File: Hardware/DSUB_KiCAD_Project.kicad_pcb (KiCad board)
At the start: 4 copper layers, 112.2 x 87.2 mm, 6 parts, among them J1 DB37_Female, J11 DB37_Female, J3 DB37_Female, J5 DB37_Female, J7 DB37_Female, J9 DB37_Female

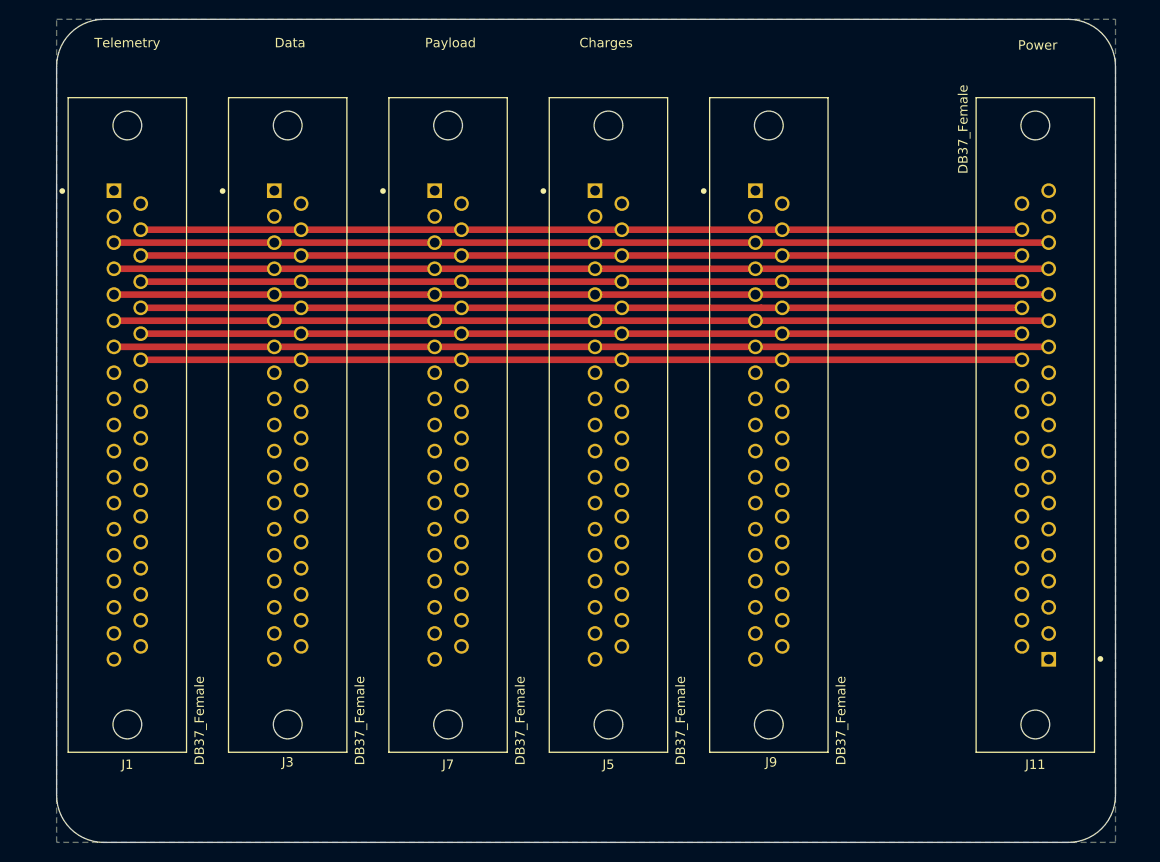
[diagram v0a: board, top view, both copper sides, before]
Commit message: Added more silk screen artwork
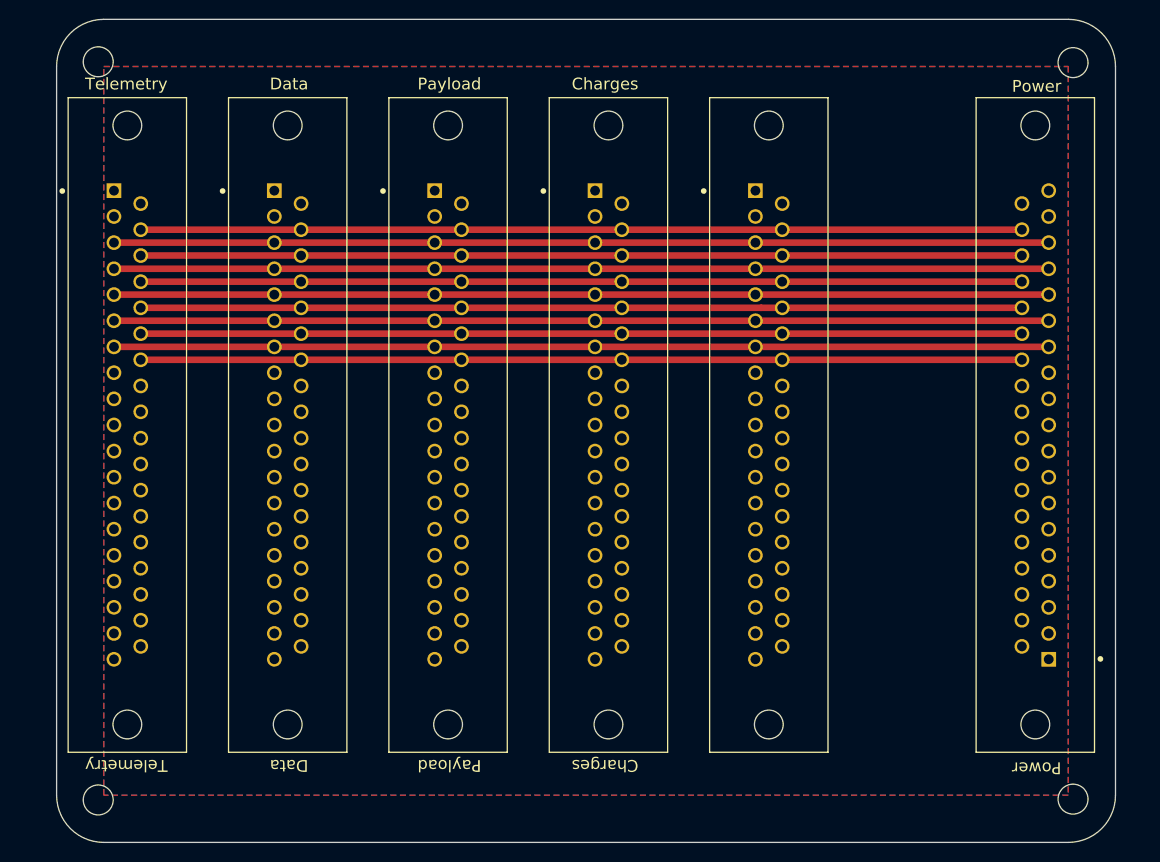
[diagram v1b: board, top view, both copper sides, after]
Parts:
- added G***: LOGO, Graphics:RDT_Logo, B.Cu at (183.2, 83.2)
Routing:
- added copper zone on B.Cu, net GND
- added copper zone on F.Cu, net GND
- removed copper zone on B.Cu, net +3V3
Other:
- outline, holes or cut-outs redrawn

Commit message: Added GND vias and copper pours
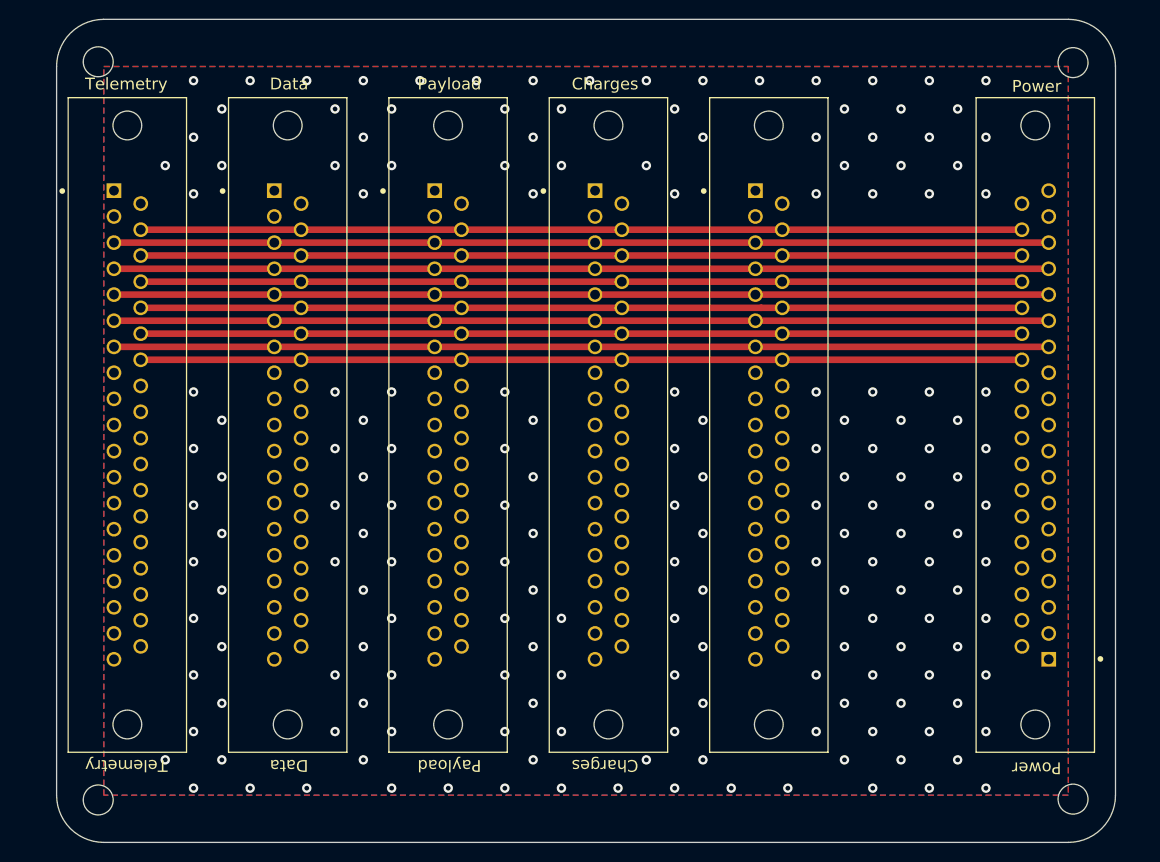
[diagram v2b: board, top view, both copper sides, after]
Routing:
- net GND: vias 0 -> 179
- added copper zone on 5v, net GND
- removed copper zone on 5v, net +5V

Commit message: changed dimensions
dimensions of the board was changed
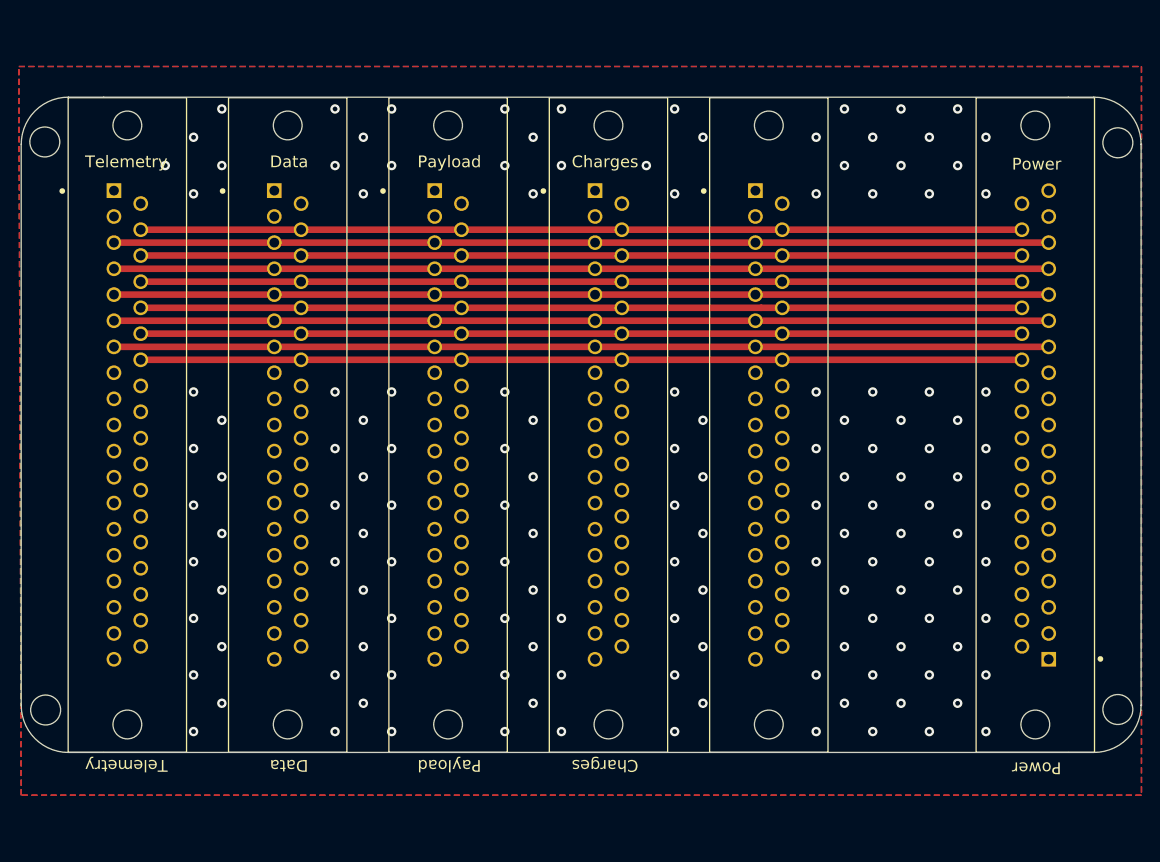
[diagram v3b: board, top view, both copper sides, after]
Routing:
- net GND: vias 179 -> 141
- added copper zone on In2.Cu, net +3V3
- added copper zone on In1.Cu, net +5V
- removed copper zone on 5v, net GND
- removed copper zone on Ground, net GND
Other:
- board size 112.2 x 87.2 mm -> 118.7 x 69.5 mm
- net class Default removed
